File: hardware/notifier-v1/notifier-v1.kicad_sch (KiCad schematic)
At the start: 0 parts

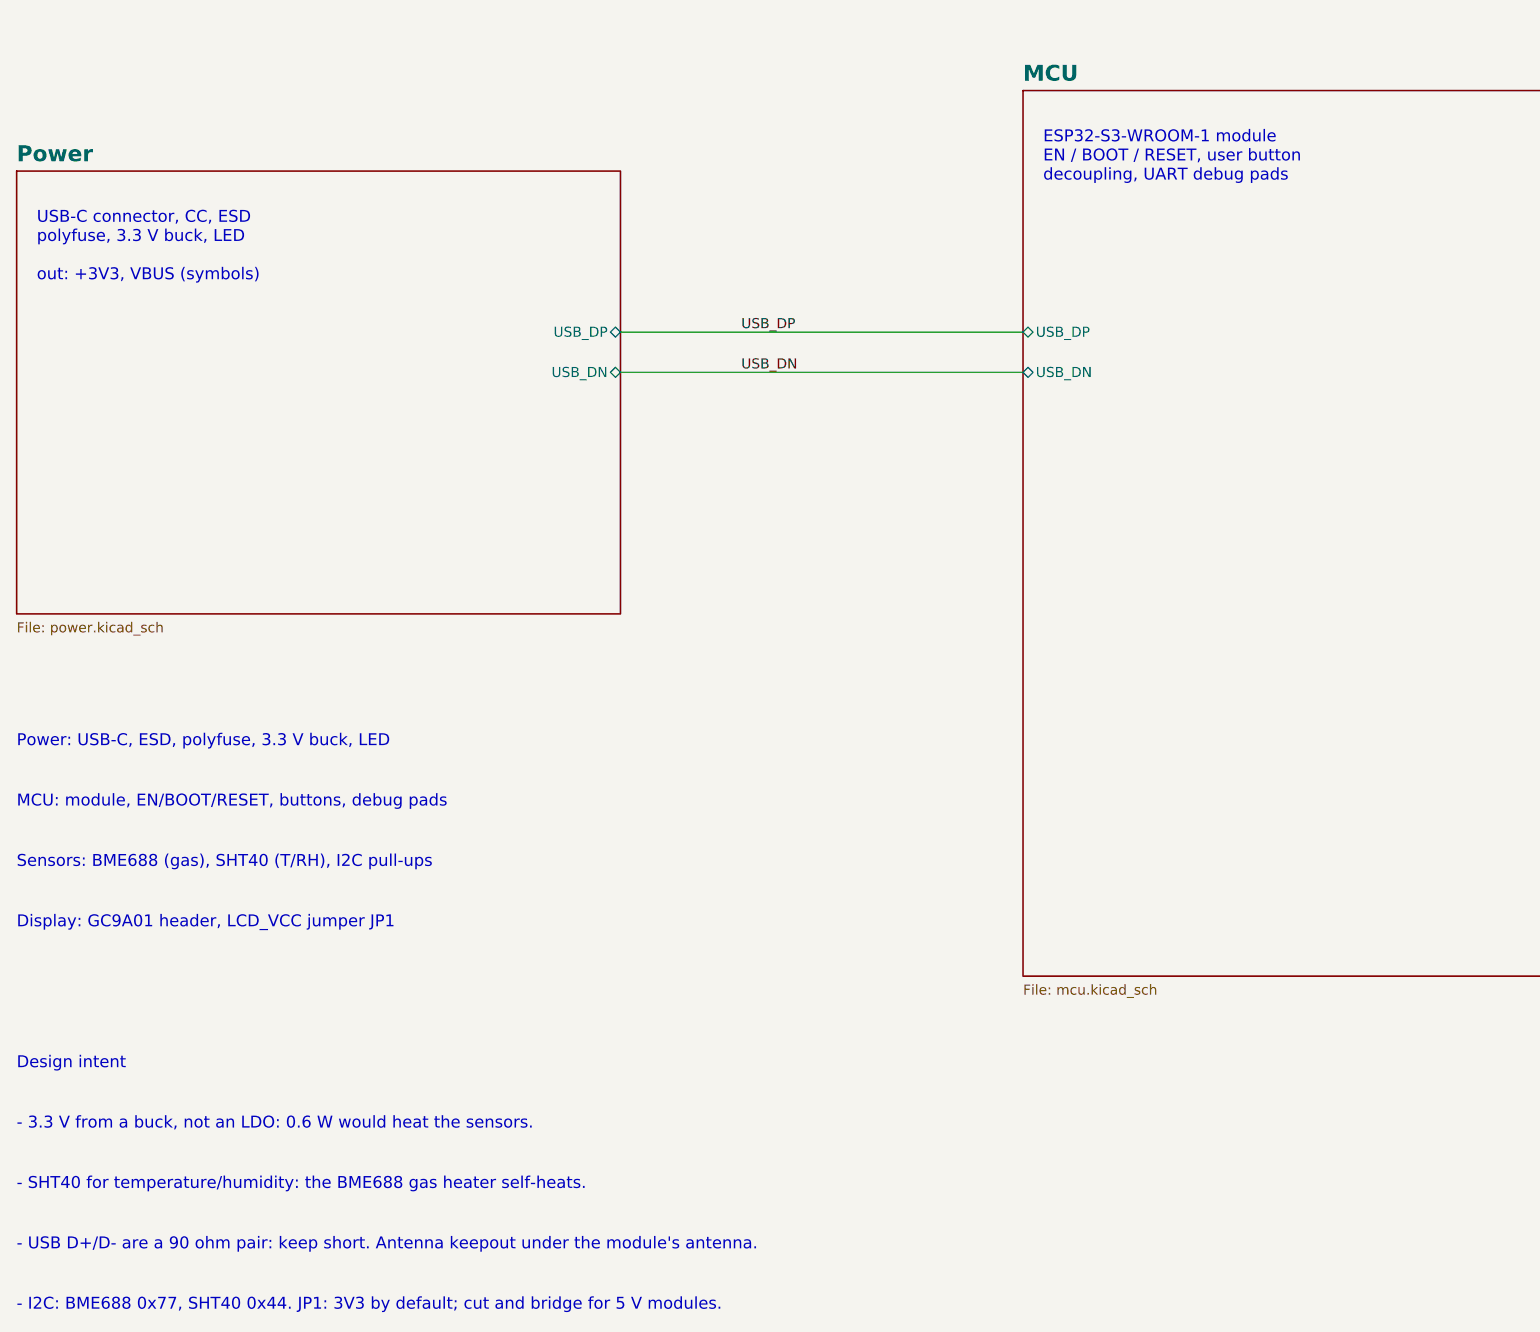
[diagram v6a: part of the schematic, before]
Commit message: Layout A: USB-C on the back edge, corner mounts, no buttons, JLC fab data
- J2 display socket mirrored (1 RST 2 CS 3 DC 4 SDA 5 SCL 6 GND 7 VCC),
  face at the right edge
- USB-C J1 on the left edge (enclosure back), ESD/CC/fuse beside it,
  hand-drawn 0.27/0.15 pair (~91 ohm diff, tools/impedance.py), only
  GND under the shell (DRC rule area)
- SW1-SW3/R6/BTN removed; 1.5 mm debug pads TX RX 3V3 EN GND IO0;
  firmware DESK_BTN = -1 on notifier-v1
- Four M2 corner holes with keepouts; sensor island grown to 14.8 mm
  with H3 in its corner, re-hand-routed (BME688/SHT40 8.9 mm apart)
- I2C >= 1.6 mm from USB on the same layer; vias >= 0.15 mm from
  same-net SMD pads (rule), hand vias >= 0.2 mm
- Silk "v1 ${GIT_SHA}" resolved at fab export; JLC order-number mark
- Fab: Protel gerbers without X2, PTH/NPTH split, JLC BOM/CPL, CPL
  rotation fixes (U4 +90, U5 +270); pipeline --fab-only on a clean
  commit; route retry until the gate passes
- ORDER.md: stackup JLC04161H-7628, rails left/right, preview checklist,
  bring-up without buttons; PLAN.md enclosure notes

Co-Authored-By: Claude Opus 5.5 <noreply@anthropic.com>
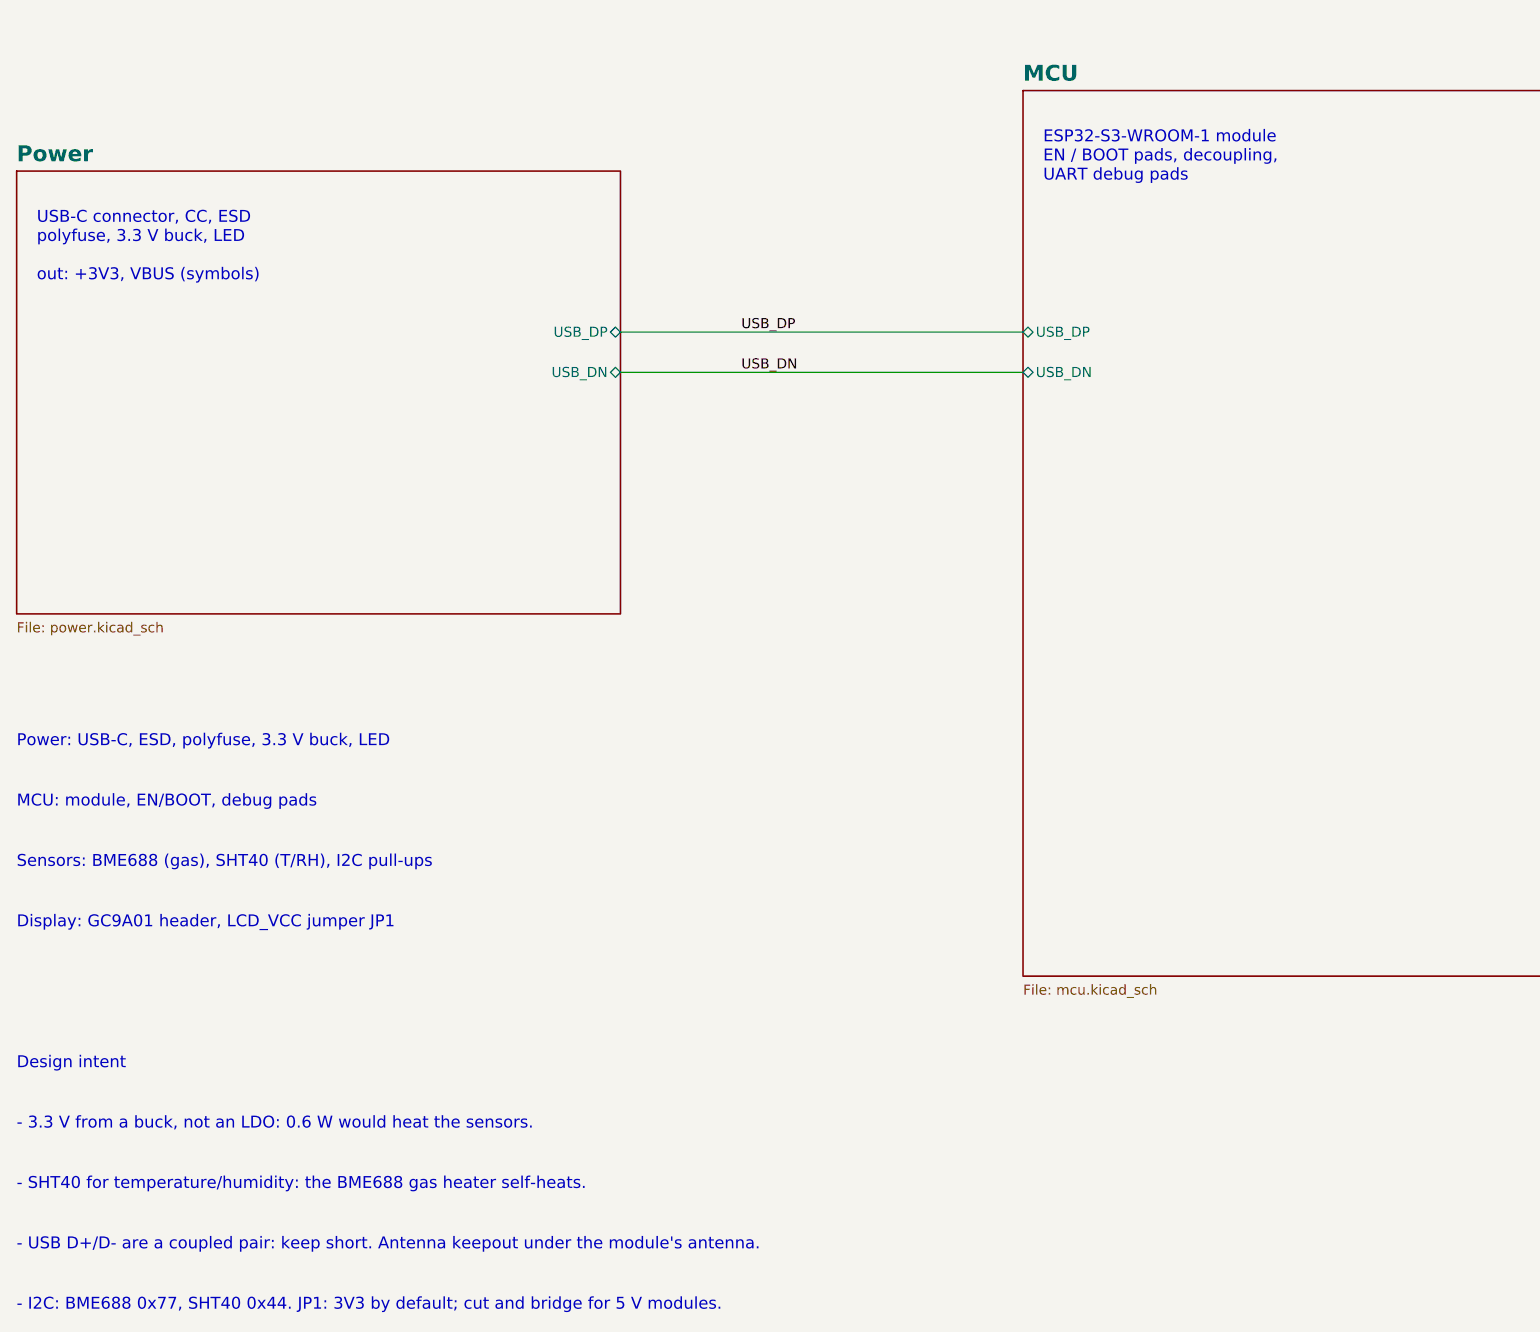
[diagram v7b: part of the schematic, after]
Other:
- note added: "- USB D+/D- are a coupled pair: keep short. Antenna keepout under the module's antenna."
- note added: "ESP32-S3-WROOM-1 module EN / BOOT pads, decoupling, UART debug pads"
- note added: "MCU: module, EN/BOOT, debug pads"
- note removed: "- USB D+/D- are a 90 ohm pair: keep short. Antenna keepout under the module's antenna."
- note removed: "ESP32-S3-WROOM-1 module EN / BOOT / RESET, user button decoupling, UART debug pads"
- note removed: "MCU: module, EN/BOOT/RESET, buttons, debug pads"
